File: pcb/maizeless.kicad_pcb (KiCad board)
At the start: 2 copper layers, 129.8 x 90 mm, 25 parts, among them SW1 SW_PUSH, SW10 SW_PUSH, SW11 SW_PUSH, SW12 SW_PUSH, SW13 SW_PUSH, SW14 SW_PUSH, SW15 SW_PUSH, SW16 SW_PUSH, SW17 SW_PUSH, SW18 SW_PUSH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

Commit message: Route
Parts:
- added battery_route: , , F.Cu at (170.2, 56.1)
- u1: renamed from U1; value nice_nano -> SuperMini
- moved BT1 27.1 mm to (175.6, 70.4)
- moved RSW1 6.77 mm to (174.3, 100.8)
- moved PWR_SW1 6.27 mm to (183.6, 104.1)
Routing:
- net key13: track 0.00 -> 142.8 mm
- net key14: track 0.00 -> 116.6 mm
- net key1: track 0.00 -> 111.4 mm
- net key7: track 0.00 -> 107.7 mm
- net key8: track 0.00 -> 97.6 mm
- net key2: track 0.00 -> 91.7 mm
- net key15: track 0.00 -> 87.7 mm
- net key9: track 0.00 -> 75.3 mm
- net key3: track 0.00 -> 70.1 mm
- net key16: track 0.00 -> 66.2 mm
- net key4: track 0.00 -> 56.8 mm
- net key10: track 0.00 -> 54.7 mm
- net key17: track 0.00 -> 49.9 mm
- net key11: track 0.00 -> 49.2 mm
- net thumb1: track 0.00 -> 48.2 mm
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
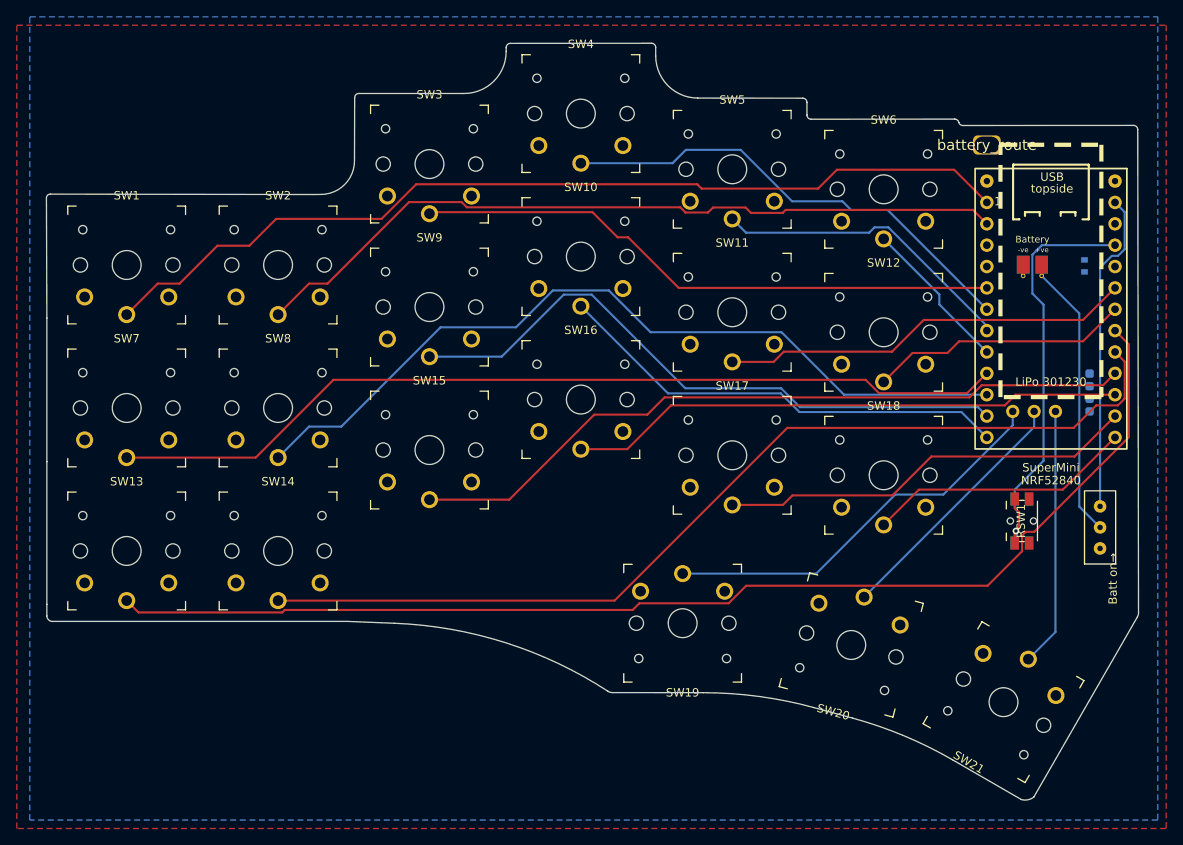
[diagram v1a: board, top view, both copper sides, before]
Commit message: Shift thumb3, remove switch labels
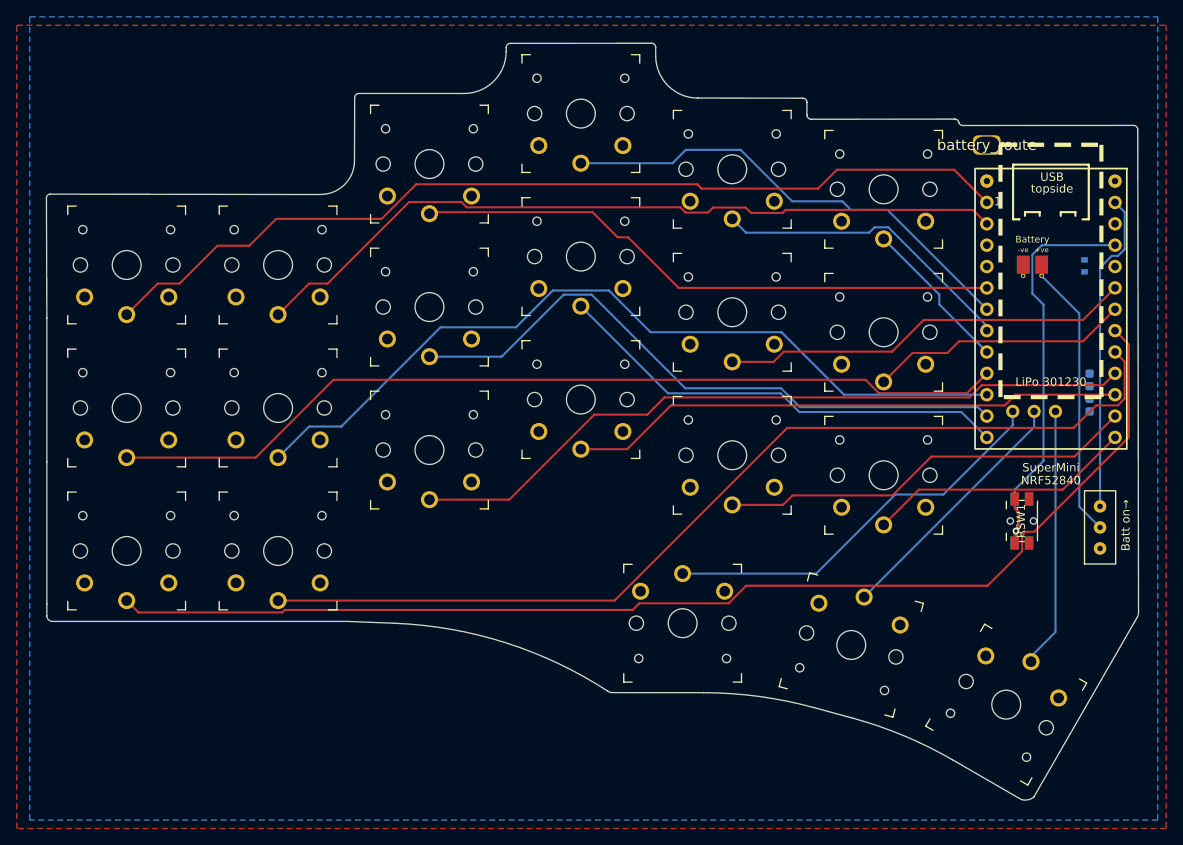
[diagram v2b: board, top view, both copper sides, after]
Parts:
- moved SW21 0.44 mm to (172.5, 122.7)
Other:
- board text added: "+ve"
- board text added: "-ve"
- board text added: "Battery"

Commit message: Route and fix DRC errors
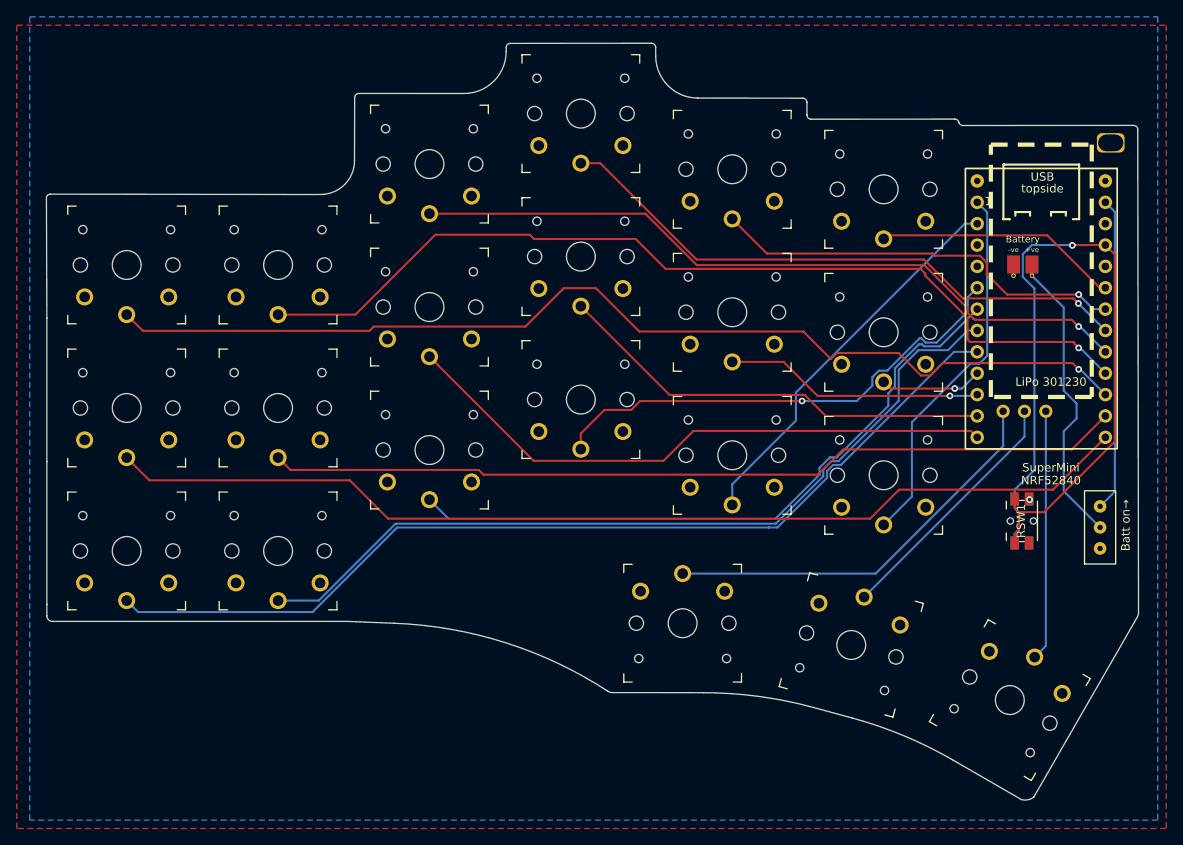
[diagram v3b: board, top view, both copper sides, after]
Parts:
- removed battery_route: , 
- added REF**: routing_via, lib:routing_via, F.Cu at (184.9, 55.9)
- u1: value SuperMini -> nice_nano
- moved BT1 1.15 mm to (174.5, 70.3)
- moved u1 1.15 mm to (169.0, 60.4)
- moved SW21 0.69 mm to (172.9, 122.1)
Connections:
- u1 pad 1: key1 -> key18
- u1 pad 10: key8 -> key11
- u1 pad 11: key9 -> key10
- u1 pad 12: key10 -> key9
- u1 pad 17: key11 -> key6
- u1 pad 18: key12 -> key5
- u1 pad 19: key13 -> key4
- u1 pad 2: key2 -> key17
- u1 pad 20: key14 -> key3
- u1 pad 21: key15 -> key2
- u1 pad 22: key16 -> key1
- u1 pad 23: key17 -> key8
- u1 pad 24: key18 -> key7
- u1 pad 5: key3 -> key16
- u1 pad 6: key4 -> key15
- u1 pad 7: key5 -> key14
- u1 pad 8: key6 -> key13
- u1 pad 9: key7 -> key12
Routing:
- net reset: track 52.6 -> 91.0 mm
- net key13: track 142.8 -> 115.0 mm
- net key2: track 91.7 -> 110.9 mm, vias 0 -> 1
- net key12: track 31.1 -> 12.2 mm, vias 0 -> 1
- net key11: track 49.2 -> 31.1 mm, vias 0 -> 1
- net key14: track 116.6 -> 99.1 mm
- net key3: track 70.1 -> 87.5 mm, vias 0 -> 1
- net key7: track 107.7 -> 123.4 mm
- net key1: track 111.4 -> 126.3 mm, vias 0 -> 1
- net key4: track 56.8 -> 70.6 mm, vias 0 -> 1
- net key5: track 36.6 -> 49.6 mm, vias 0 -> 1
- net key18: track 31.8 -> 44.6 mm
- net key6: track 18.5 -> 29.1 mm
- net key15: track 87.7 -> 79.2 mm
- net key16: track 66.2 -> 58.2 mm, vias 0 -> 1
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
